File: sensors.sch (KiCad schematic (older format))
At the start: 22 parts, among them Q7 IRLML2502, SW1 TL6215RF200BDT, U13 VL53L1CXV0FY/1, U14 APDS-9960, U23 LSM6DS3, U6 LIS2HH12

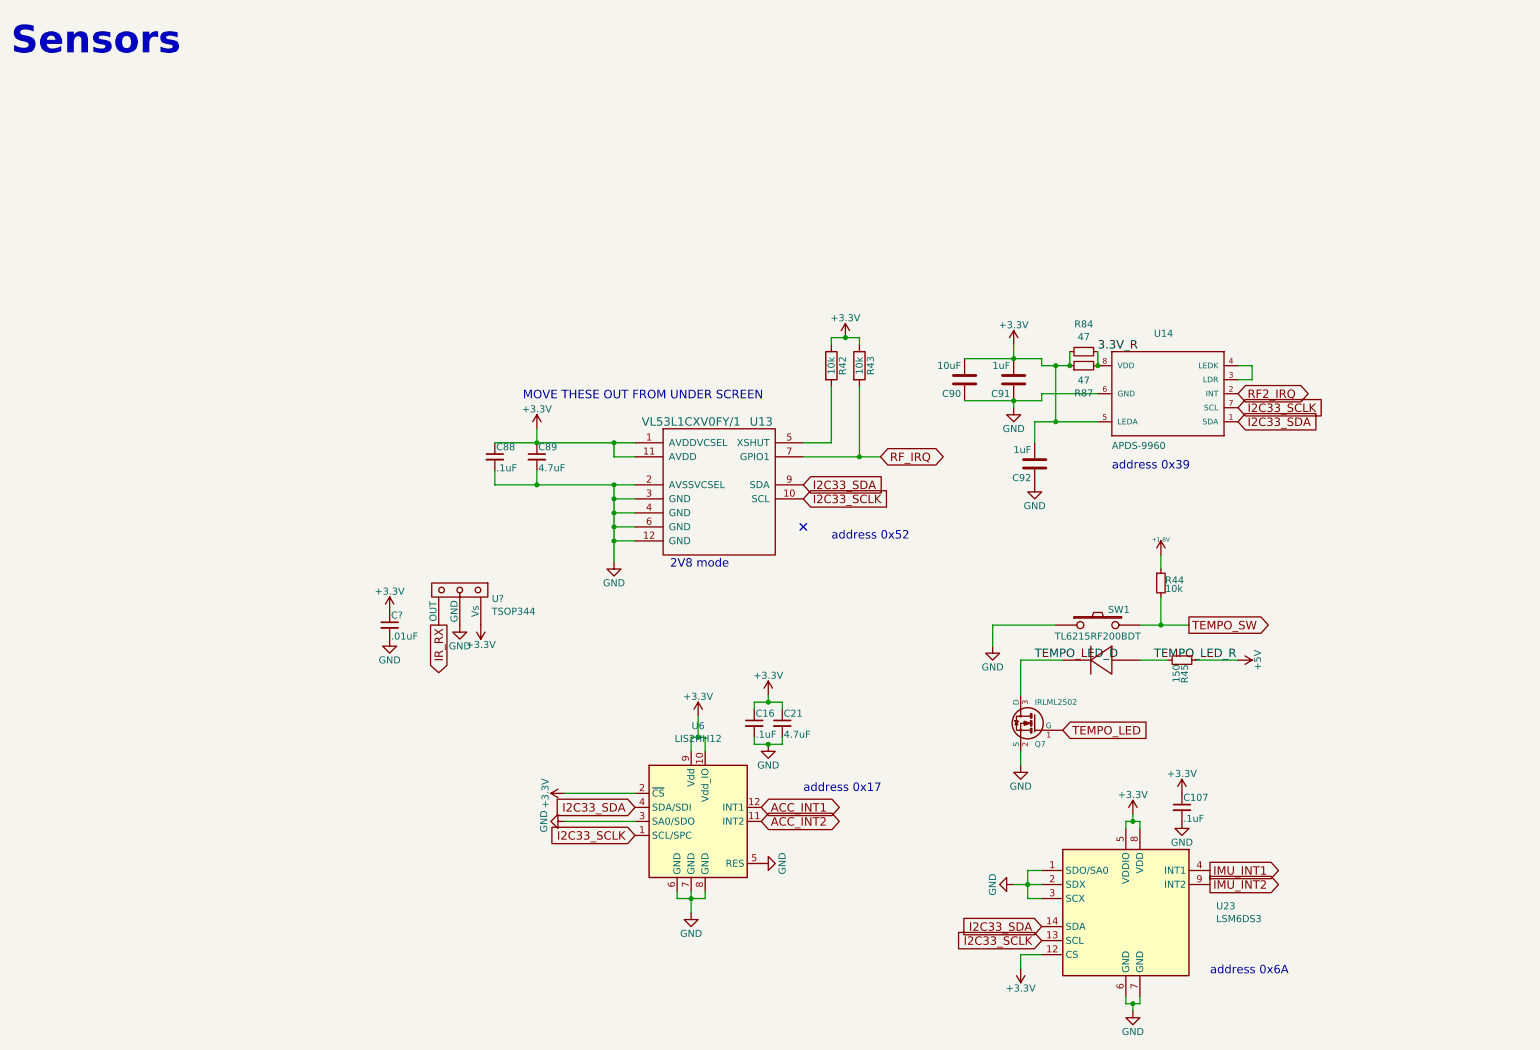
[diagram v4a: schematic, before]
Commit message: some part changes for BOM clarification
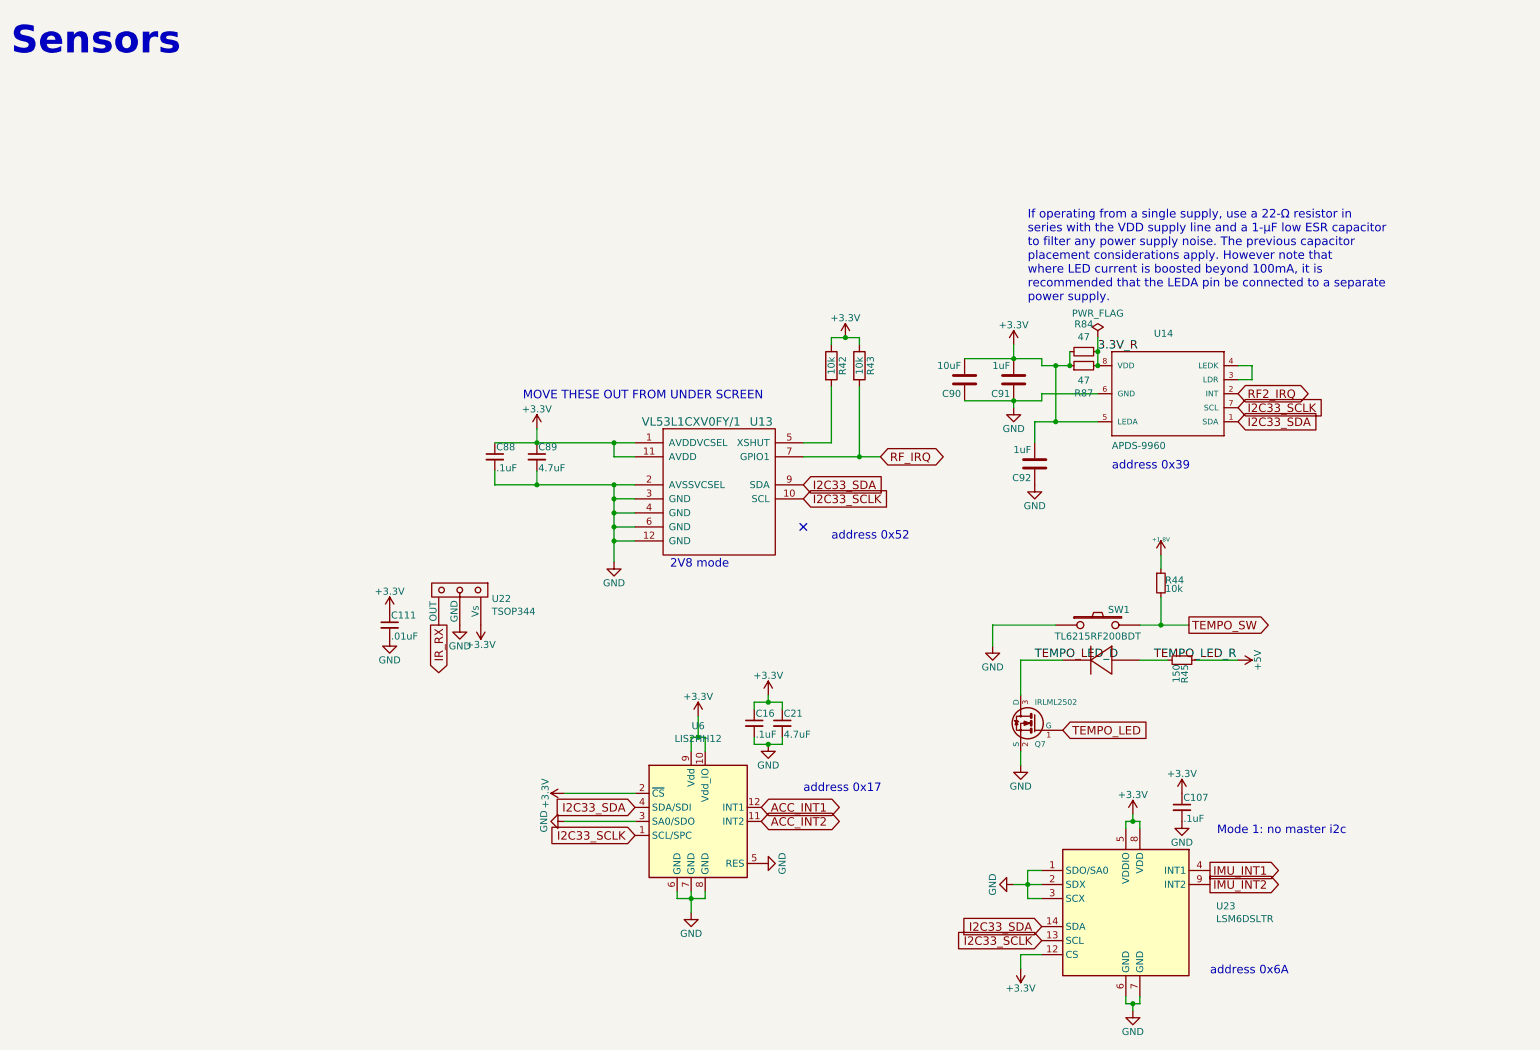
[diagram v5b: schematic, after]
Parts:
- C107, C16, C88: MFR Murata -> Yageo; MPN GRM188R71C104KA01D -> CC0402KRX7R6BB104; SPN 490-1532-1-ND -> 311-1345-1-ND
- C21, C89: MPN GRM21BR61A475KA73L -> GRM155R60G475ME47D; SPN 490-9750-1-ND -> 490-11980-1-ND
- C90: MPN GRM21BR61A106KE19L -> GRM188R61A106KE69J; SPN 490-1709-1-ND -> 490-14372-1-ND
- C91, C92: MFR Murata -> Yageo; MPN GRM188R71C105KE15D -> CC0402KRX5R6BB105; SPN 490-10734-1-ND -> 311-1439-1-ND
- U23: value LSM6DS3 -> LSM6DSLTR; MPN LSM6DS3TR -> LSM6DSLTR; SPN 497-15383-1-ND -> 497-16705-6-ND
- gave numbers to parts that had none: 2
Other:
- note added: "If operating from a single supply, use a 22-Ω resistor in\nseries with the VDD supply line and a 1-μF low ESR capacitor \nto filter any power supply noise. The previous capacitor \nplacement considerations apply. However note that\nwhere LED current is boosted beyond 100mA, it is \nrecommended that the LEDA pin be connected to a separate\npower supply."
- note added: "Mode 1: no master i2c"
